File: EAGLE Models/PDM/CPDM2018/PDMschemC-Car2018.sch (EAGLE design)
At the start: 26 parts

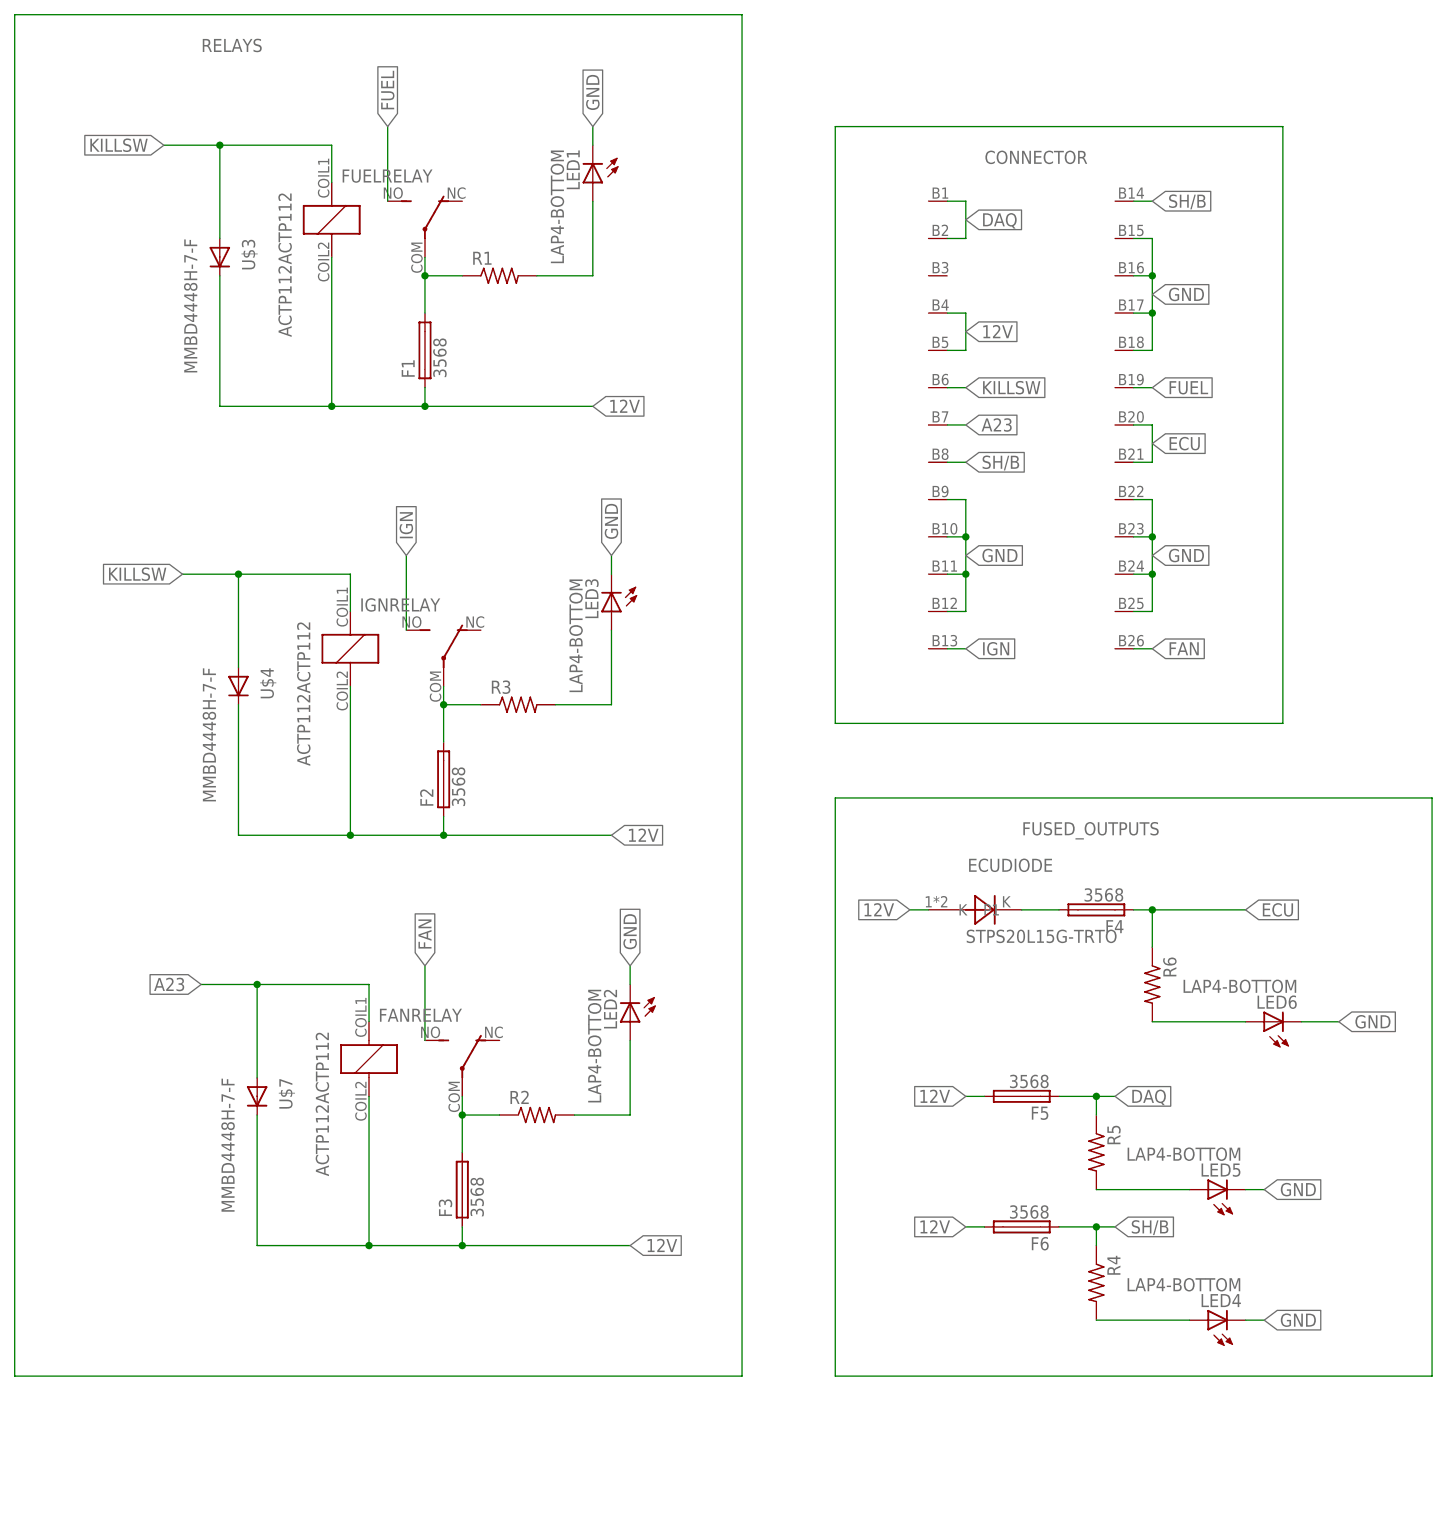
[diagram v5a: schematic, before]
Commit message: Rearranged resistors and LEDs
Rearranged LEDs and resistors so that the LEDs would be as close as possible to each fuse block.
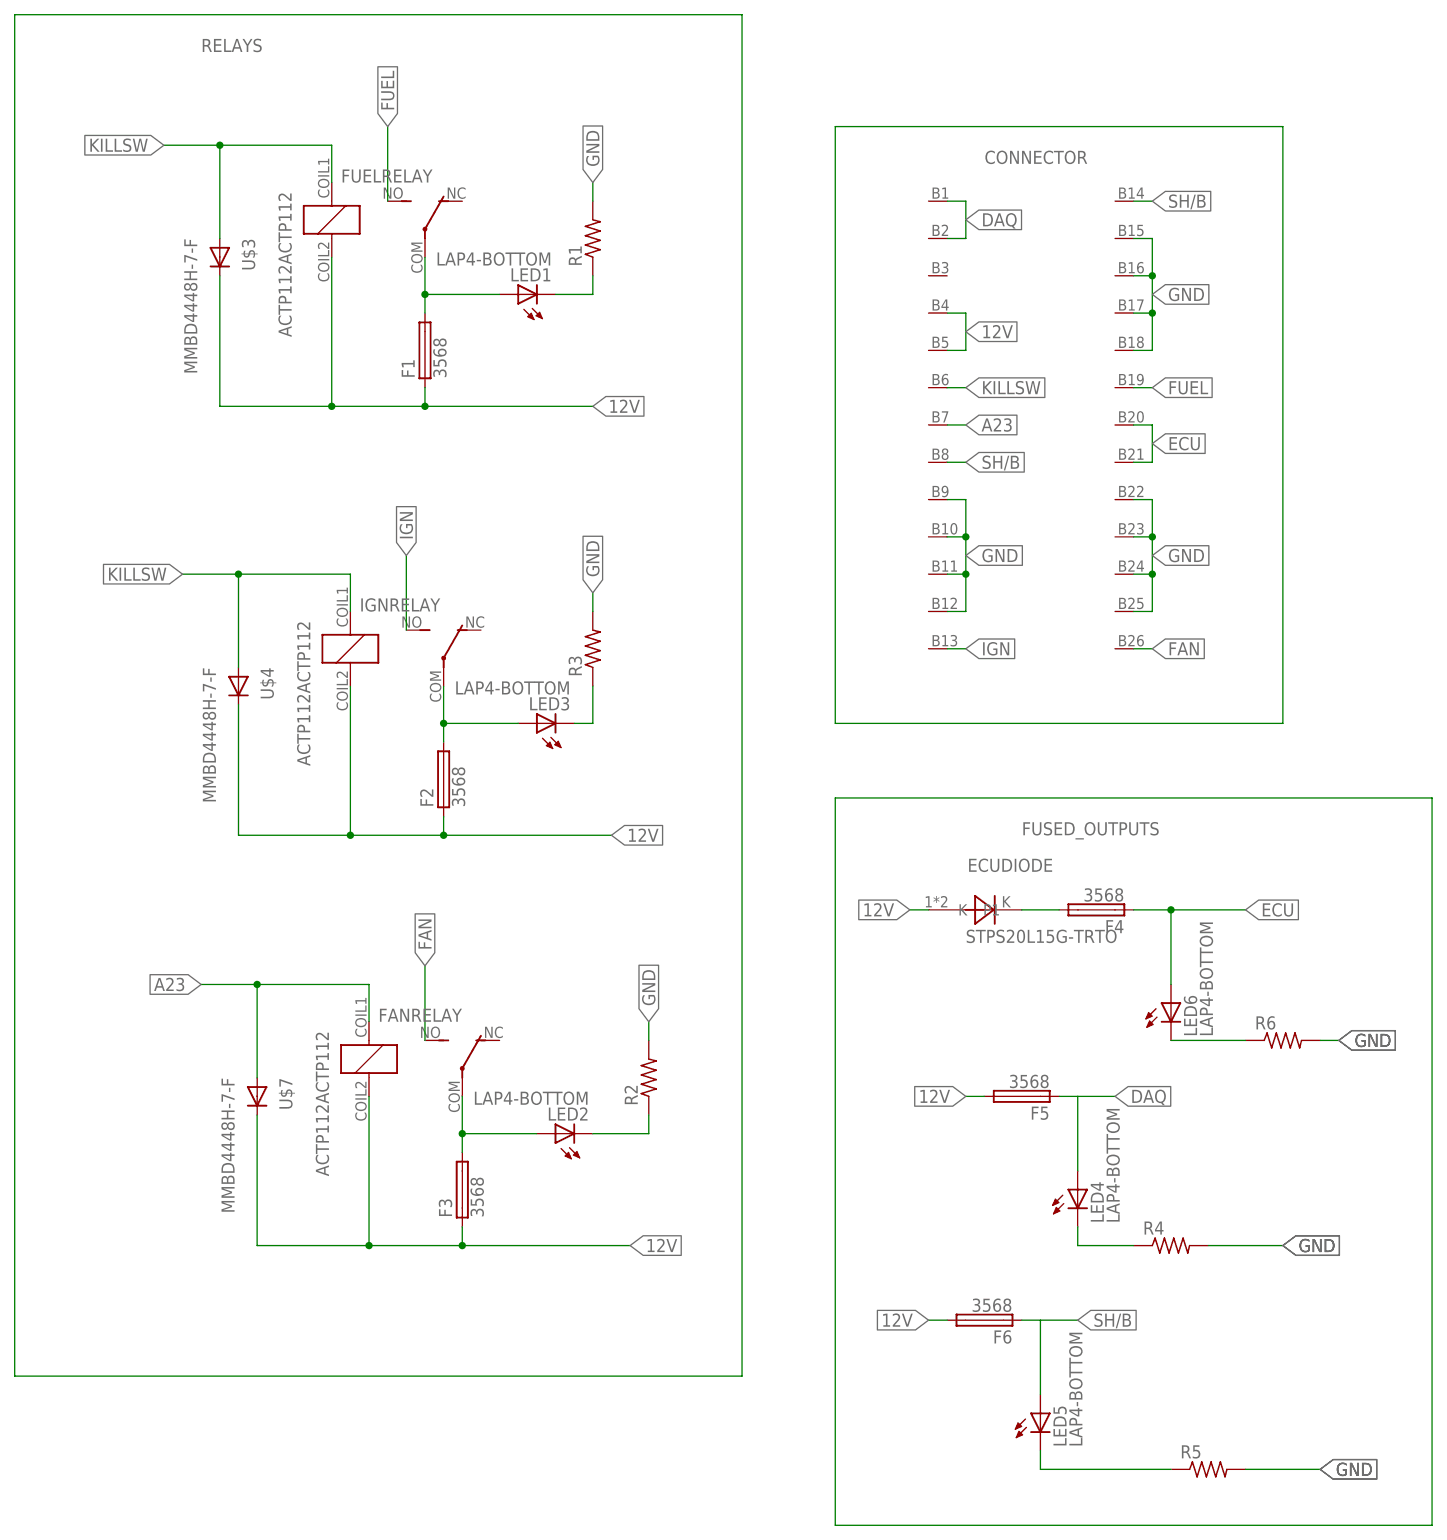
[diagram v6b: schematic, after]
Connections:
- net DAQ: now also LED4.A; no longer R5.1
- net ECU: now also LED6.A; no longer R6.1
- net GND: now also R1.2, R2.2, R3.2, R4.2, R5.2, R6.2; no longer LED1.C, LED2.C, LED3.C, LED4.C, LED5.C, LED6.C
- net N$1: now also LED2.A; no longer R2.1
- net N$10: now also LED5.C, R5.1; no longer LED5.A, R5.2
- net N$2: now also LED1.C, R1.1; no longer LED1.A, R1.2
- net N$3: now also LED1.A; no longer R1.1
- net N$4: now also LED2.C, R2.1; no longer LED2.A, R2.2
- net N$5: now also LED3.C, R3.1; no longer LED3.A, R3.2
- net N$6: now also LED3.A; no longer R3.1
- net N$7: now also LED4.C, R4.1; no longer LED4.A, R4.2
- net N$8: now also LED6.C, R6.1; no longer LED6.A, R6.2
- net SH/B: now also LED5.A; no longer R4.1
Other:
- moved on the sheet: F6, LED1, LED2, LED3, LED4, LED5, LED6, R1, R2, R3, R4, R5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

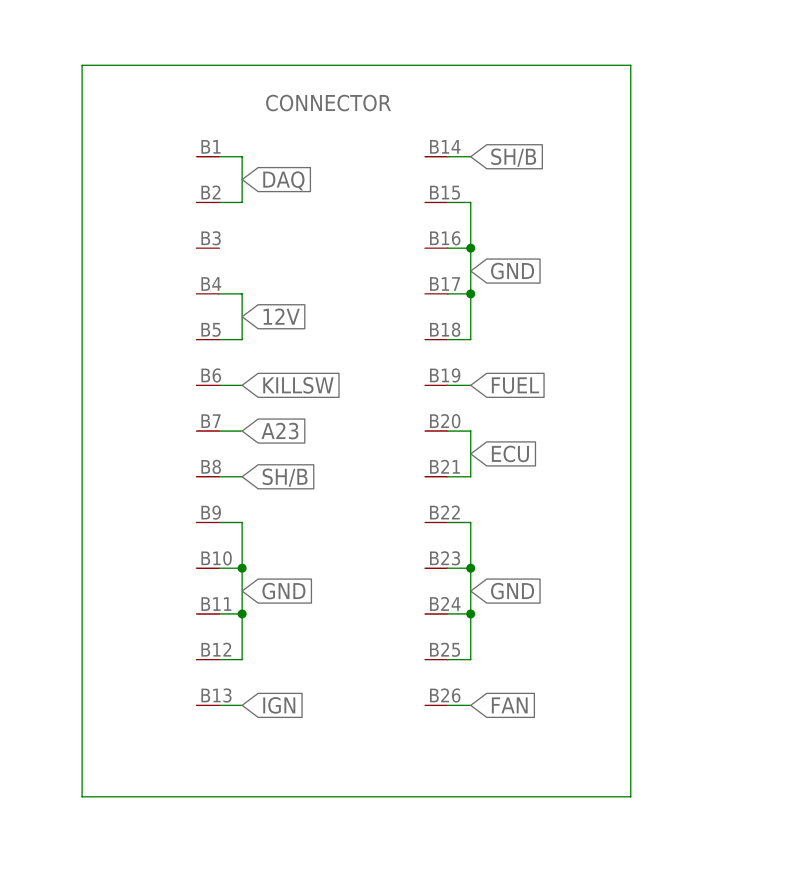
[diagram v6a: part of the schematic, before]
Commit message: Began routing traces
Started creating traces for the PDM. Switched several pins on the connector to help create those traces.
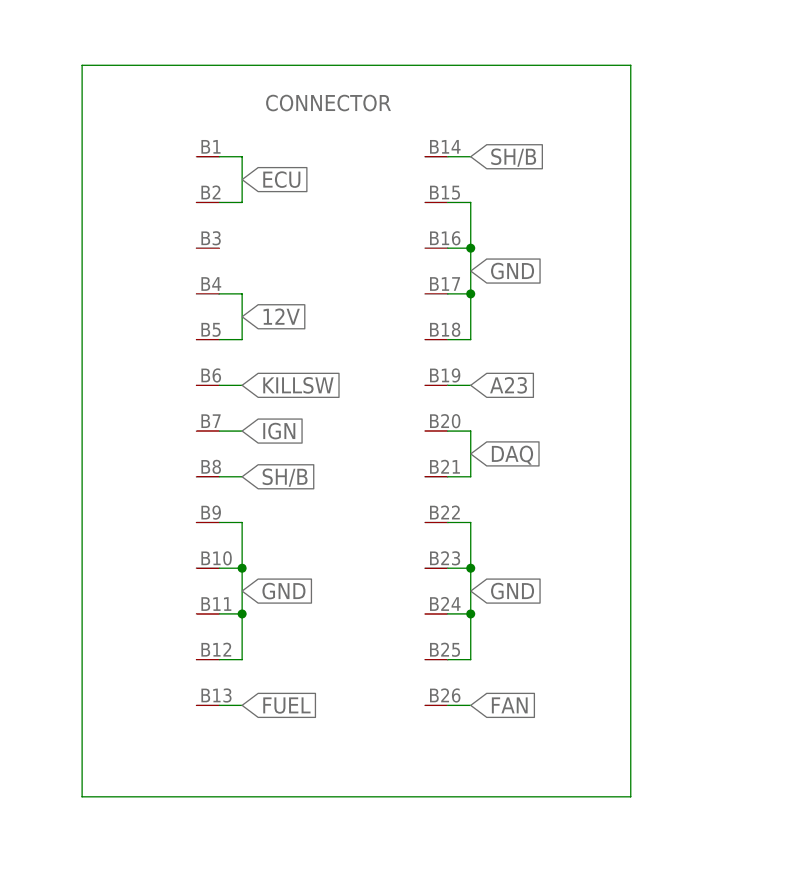
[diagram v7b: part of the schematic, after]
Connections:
- net A23: now also U$1.B19; no longer U$1.B7
- net DAQ: now also U$1.B20, U$1.B21; no longer U$1.B1, U$1.B2
- net ECU: now also U$1.B1, U$1.B2; no longer U$1.B20, U$1.B21
- net FUEL: now also U$1.B13; no longer U$1.B19
- net IGN: now also U$1.B7; no longer U$1.B13
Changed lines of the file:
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@@
 <net name="IGN" class="0">
+<segment>
+<pinref part="IGNRELAY" gate="G$1" pin="NO"/>
+<wire x1="121.92" y1="91.44" x2="121.92" y2="101.6" width="0.1524" layer="91"/>
+<label x="121.92" y="101.6" size="1.778" layer="95" rot="R90" xref="yes"/>
+</segment>
+<segment>
+<pinref part="U$1" gate="G$1" pin="B7"/>
+<wire x1="195.58" y1="119.38" x2="198.12" y2="119.38" width="0.1524" layer="91"/>
+<label x="198.12" y="119.38" size="1.778" layer="95" xref="yes"/>
+</segment>
+</net>
+<net name="FUEL" class="0">
+<segment>
+<pinref part="FUELRELAY" gate="G$1" pin="NO"/>
+<wire x1="119.38" y1="149.86" x2="119.38" y2="160.02" width="0.1524" layer="91"/>
+<label x="119.38" y="160.02" size="1.778" layer="95" rot="R90" xref="yes"/>
+</segment>
 <segment>
 <pinref part="U$1" gate="G$1" pin="B13"/>
 <wire x1="195.58" y1="88.9" x2="198.12" y2="88.9" width="0.1524" layer="91"/>
 <label x="198.12" y="88.9" size="1.778" layer="95" xref="yes"/>
-</segment>
-<segment>
-<pinref part="IGNRELAY" gate="G$1" pin="NO"/>
-<wire x1="121.92" y1="91.44" x2="121.92" y2="101.6" width="0.1524" layer="91"/>
-<label x="121.92" y="101.6" size="1.778" layer="95" rot="R90" xref="yes"/>
-</segment>
-</net>
-<net name="FUEL" class="0">
-<segment>
-<pinref part="U$1" gate="G$1" pin="B19"/>
-<wire x1="220.98" y1="124.46" x2="223.52" y2="124.46" width="0.1524" layer="91"/>
-<label x="223.52" y="124.46" size="1.778" layer="95" xref="yes"/>
-</segment>
-<segment>
-<pinref part="FUELRELAY" gate="G$1" pin="NO"/>
-<wire x1="119.38" y1="149.86" x2="119.38" y2="160.02" width="0.1524" layer="91"/>
-<label x="119.38" y="160.02" size="1.778" layer="95" rot="R90" xref="yes"/>
 </segment>
 </net>
@@
 </segment>
 <segment>
-<pinref part="U$1" gate="G$1" pin="B1"/>
-<wire x1="195.58" y1="149.86" x2="198.12" y2="149.86" width="0.1524" layer="91"/>
-<pinref part="U$1" gate="G$1" pin="B2"/>
-<wire x1="195.58" y1="144.78" x2="198.12" y2="144.78" width="0.1524" layer="91"/>
-<wire x1="198.12" y1="149.86" x2="198.12" y2="144.78" width="0.1524" layer="91"/>
-<label x="198.12" y="147.32" size="1.778" layer="95" xref="yes"/>
-</segment>
-<segment>
 <pinref part="LED4" gate="G$1" pin="A"/>
 <wire x1="213.36" y1="27.94" x2="213.36" y2="17.78" width="0.1524" layer="91"/>
+</segment>
+<segment>
+<pinref part="U$1" gate="G$1" pin="B20"/>
+<wire x1="220.98" y1="119.38" x2="223.52" y2="119.38" width="0.1524" layer="91"/>
+<pinref part="U$1" gate="G$1" pin="B21"/>
+<wire x1="220.98" y1="114.3" x2="223.52" y2="114.3" width="0.1524" layer="91"/>
+<wire x1="223.52" y1="119.38" x2="223.52" y2="114.3" width="0.1524" layer="91"/>
+<label x="223.52" y="116.84" size="1.778" layer="95" xref="yes"/>
 </segment>
 </net>
@@
 </segment>
 <segment>
-<pinref part="U$1" gate="G$1" pin="B20"/>
-<wire x1="220.98" y1="119.38" x2="223.52" y2="119.38" width="0.1524" layer="91"/>
-<pinref part="U$1" gate="G$1" pin="B21"/>
-<wire x1="220.98" y1="114.3" x2="223.52" y2="114.3" width="0.1524" layer="91"/>
-<wire x1="223.52" y1="119.38" x2="223.52" y2="114.3" width="0.1524" layer="91"/>
-<label x="223.52" y="116.84" size="1.778" layer="95" xref="yes"/>
+<pinref part="U$1" gate="G$1" pin="B1"/>
+<wire x1="195.58" y1="149.86" x2="198.12" y2="149.86" width="0.1524" layer="91"/>
+<pinref part="U$1" gate="G$1" pin="B2"/>
+<wire x1="195.58" y1="144.78" x2="198.12" y2="144.78" width="0.1524" layer="91"/>
+<wire x1="198.12" y1="149.86" x2="198.12" y2="144.78" width="0.1524" layer="91"/>
+<label x="198.12" y="147.32" size="1.778" layer="95" xref="yes"/>
 </segment>
 </net>
@@
 </segment>
 <segment>
-<pinref part="U$1" gate="G$1" pin="B7"/>
-<wire x1="195.58" y1="119.38" x2="198.12" y2="119.38" width="0.1524" layer="91"/>
-<label x="198.12" y="119.38" size="1.778" layer="95" xref="yes"/>
-</segment>
-</net>
+<pinref part="U$1" gate="G$1" pin="B19"/>
+<wire x1="220.98" y1="124.46" x2="223.52" y2="124.46" width="0.1524" layer="91"/>
+<label x="223.52" y="124.46" size="1.778" layer="95" xref="yes"/>
+</segment>
+</net>
